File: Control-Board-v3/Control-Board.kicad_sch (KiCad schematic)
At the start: 16 parts, among them SW1 SW_SPST, U3 WeMos_D1_mini

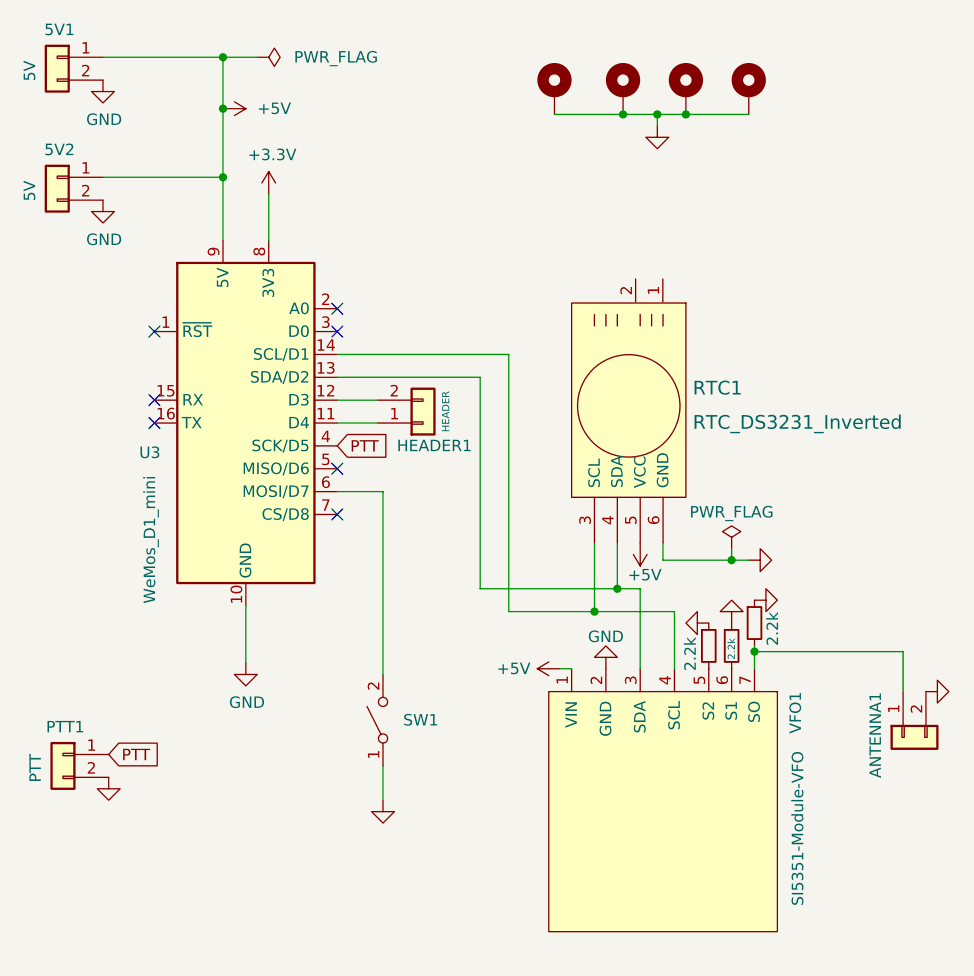
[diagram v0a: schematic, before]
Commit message: Add support for 'Custom WSPR messages'
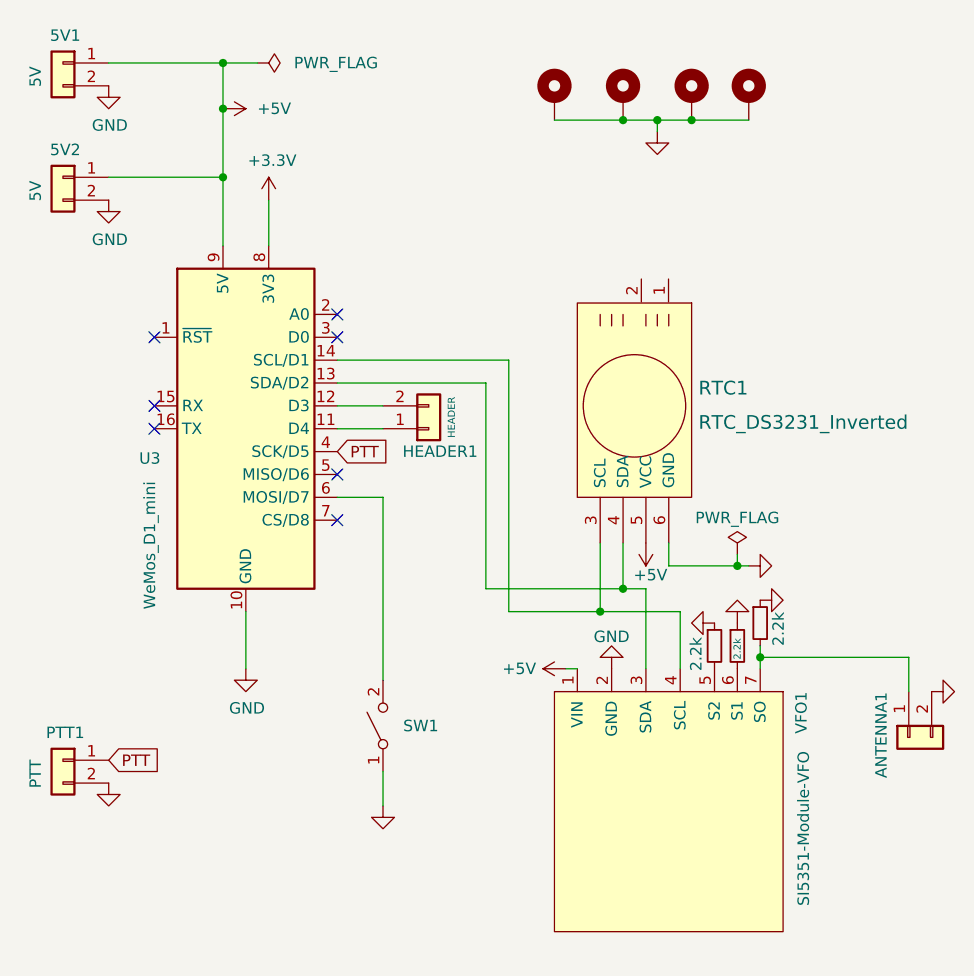
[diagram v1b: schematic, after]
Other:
- title: Easy-Digital-Beacons -> Easy-Digital-Beacons - Schematic
- moved on the sheet: 5V1, 5V2, ANTENNA1, HEADER1, PTT1, RTC1, SW1, U3, VFO1
